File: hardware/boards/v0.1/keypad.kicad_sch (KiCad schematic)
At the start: 74 parts, among them SW1 TRIG1, SW10 TRIG10, SW11 TRIG11, SW12 TRIG12, SW13 TRIG13, SW14 TRIG14, SW15 TRIG15, SW16 TRIG16, SW17 MENU0, SW18 HELP, SW19 MENU1, SW2 TRIG2, SW20 MENU2, SW21 MENU3, SW3 TRIG3, SW4 TRIG4, SW5 TRIG5, SW6 TRIG6, SW7 TRIG7, SW8 TRIG8, SW9 TRIG9, U25 TCA8418RTWR

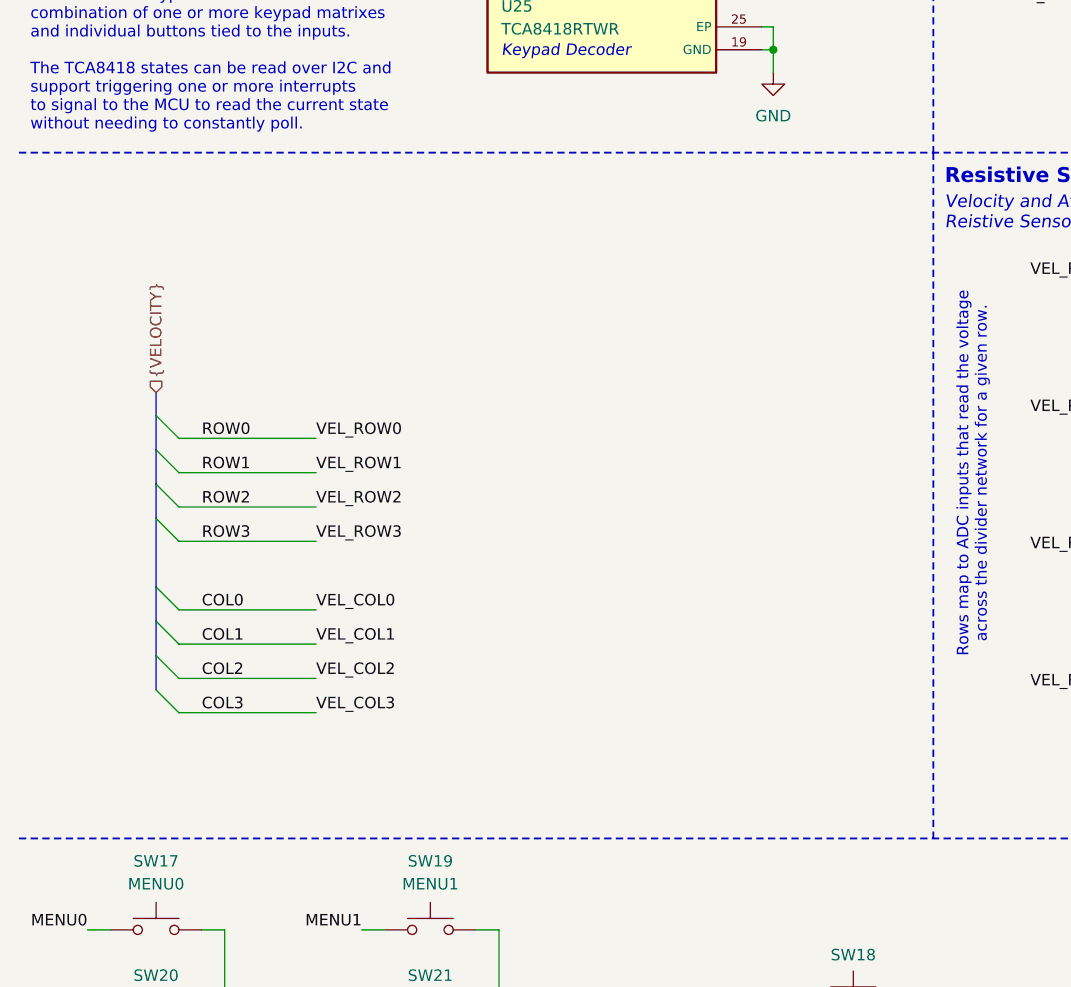
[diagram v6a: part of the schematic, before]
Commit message: feat: add IO expander for velocity pads
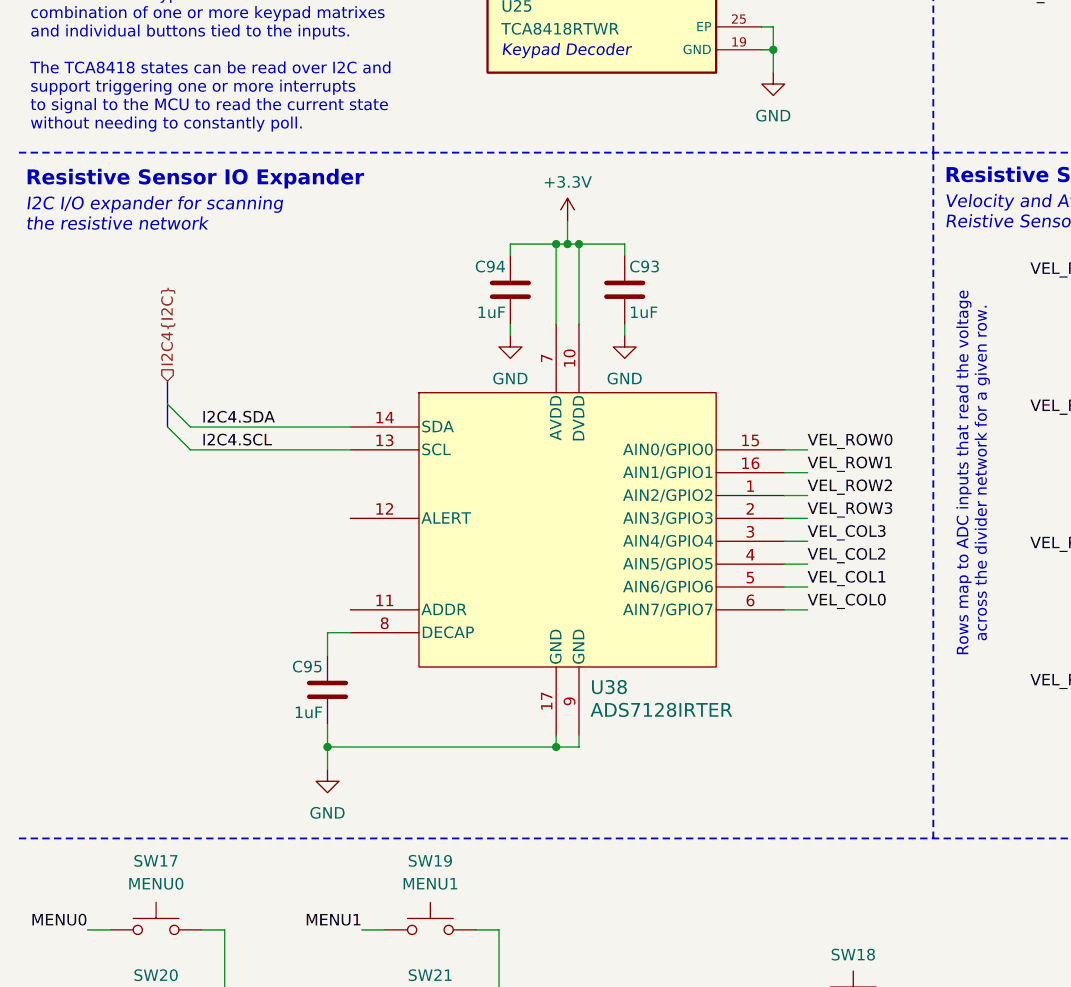
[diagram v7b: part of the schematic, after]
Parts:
- added C93, C94, C95: 1uF, Capacitor_SMD:C_0402_1005Metric, symbol Device:C
- added U38: ADS7128IRTER, pocket_synth:ADS7128IRTER, symbol pocket_synth:ADS7128IRTER
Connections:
- net +3.3V: now also C93.1, C94.1, U38.10 (DVDD), U38.7 (AVDD)
- net GND: now also C93.2, C94.2, C95.2, U38.17 (GND), U38.9 (GND)
- net I2C4.SCL: now also U38.13 (SCL)
- net I2C4.SDA: now also U38.14 (SDA)
- net COL0 renamed VEL_COL0
- net VEL_COL0: now also U38.6 (AIN7/GPIO7)
- net COL1 renamed VEL_COL1
- net VEL_COL1: now also U38.5 (AIN6/GPIO6)
- net COL2 renamed VEL_COL2
- net VEL_COL2: now also U38.4 (AIN5/GPIO5)
- net COL3 renamed VEL_COL3
- net VEL_COL3: now also U38.3 (AIN4/GPIO4)
- net ROW0 renamed VEL_ROW0
- net VEL_ROW0: now also U38.15 (AIN0/GPIO0)
- net ROW1 renamed VEL_ROW1
- net VEL_ROW1: now also U38.16 (AIN1/GPIO1)
- net ROW2 renamed VEL_ROW2
- net VEL_ROW2: now also U38.1 (AIN2/GPIO2)
- net ROW3 renamed VEL_ROW3
- net VEL_ROW3: now also U38.2 (AIN3/GPIO3)
- new net: C95.1, U38.8 (DECAP)
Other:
- note added: "I2C I/O expander for scanning the resistive network"
- note added: "Resistive Sensor IO Expander"

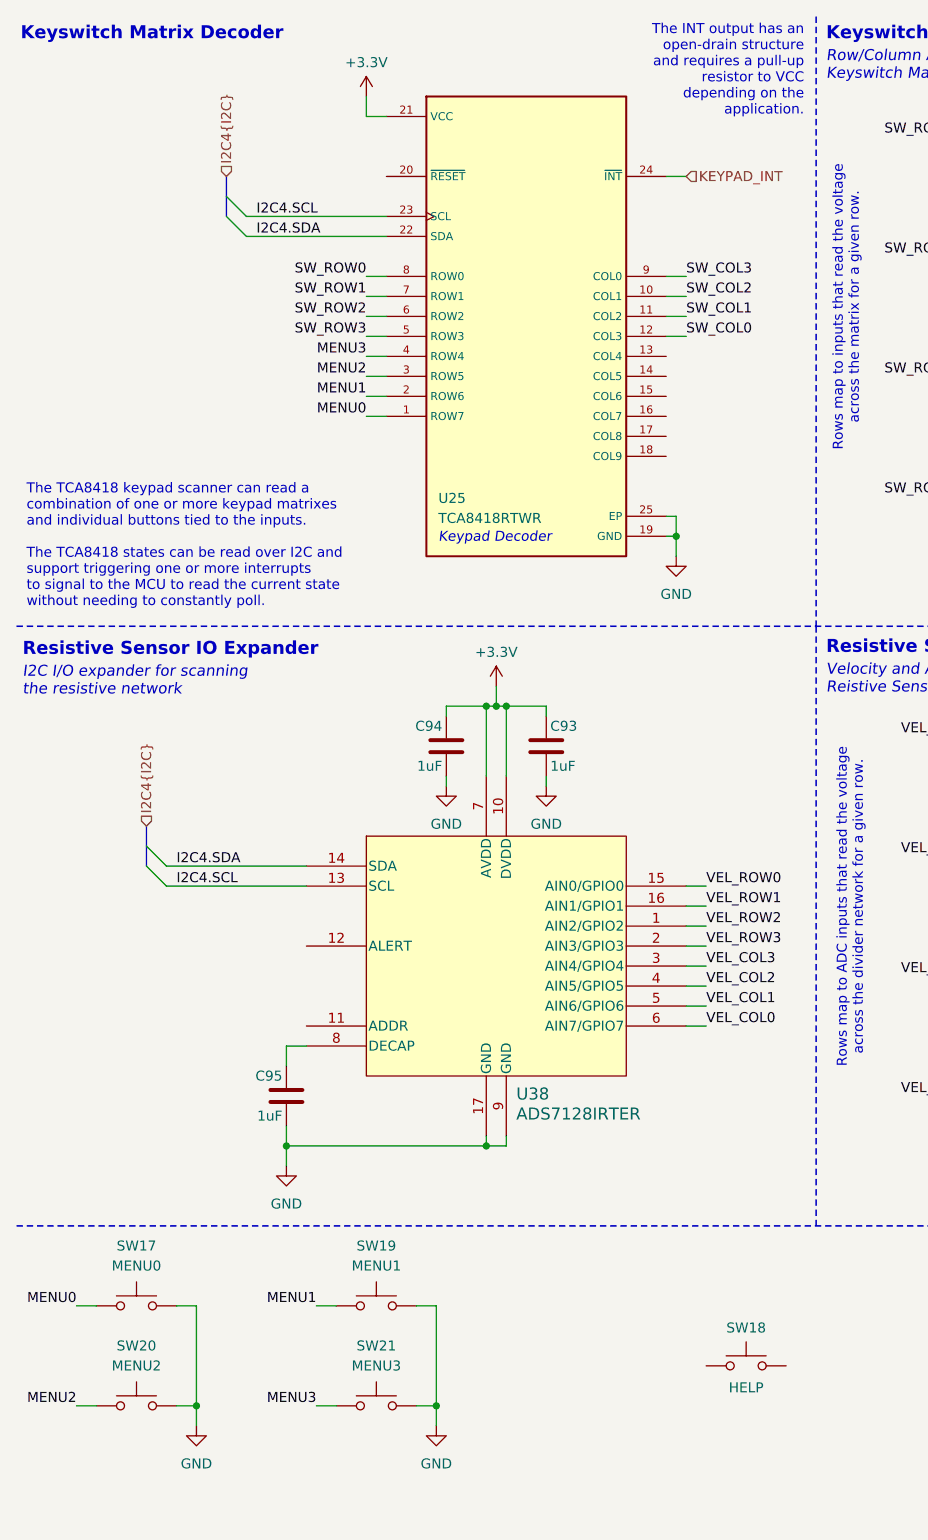
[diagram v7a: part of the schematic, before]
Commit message: feat: various ERC and DRC cleanup
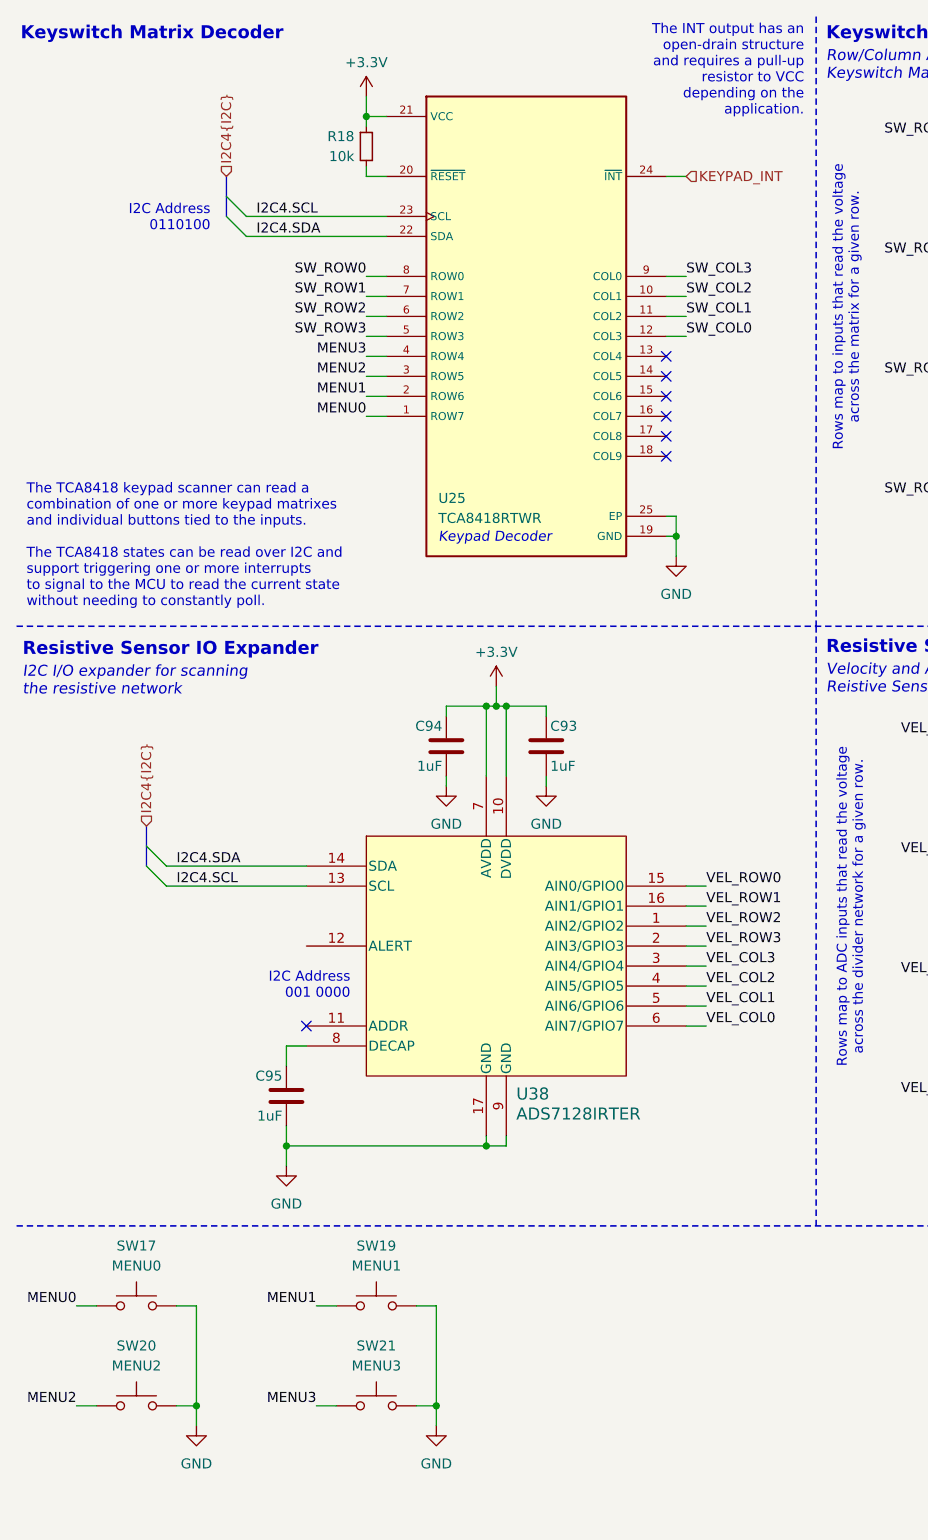
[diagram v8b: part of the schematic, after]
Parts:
- removed SW18: HELP, Button_Switch_SMD:SW_SPST_EVQQ2, symbol Switch:SW_Push
- added R18: 10k, Resistor_SMD:R_0402_1005Metric, symbol Device:R_Small
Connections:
- net +3.3V: now also R18.1
- net at U25.20 (~{RESET}): now also R18.2
- no-connect marks 0 -> 7
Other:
- note added: "I2C Address 001 0000"
- note added: "I2C Address 0110100"
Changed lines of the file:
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@@
 		)
 	)
+	(text "I2C Address\n001 0000"
+		(exclude_from_sim no)
+		(at 55.118 135.89 0)
+		(effects
+			(font
+				(size 1.27 1.27)
+				(color 132 132 132 1)
+			)
+			(justify right)
+		)
+	)
 	(text "Keyswitch Matrix Decoder"
 		(exclude_from_sim no)
@@
 		)
 	)
+	(text "I2C Address\n0110100"
+		(exclude_from_sim no)
+		(at 37.338 38.354 0)
+		(effects
+			(font
+				(size 1.27 1.27)
+				(color 132 132 132 1)
+			)
+			(justify right)
+		)
+	)
 	(text "TODO: add navigation stick?\nhttps://tech.alpsalpine.com/e/products/detail/RKJXT1F42001/#ancFig4"
 		(exclude_from_sim no)
@@
 	)
 	(junction
+		(at 57.15 25.4)
+		(diameter 0)
+		(color 0 0 0 0)
+	)
+	(junction
 		(at 135.89 43.18)
 		(diameter 0)
@@
 		(color 0 0 0 0)
 	)
+	(no_connect
+		(at 95.25 58.42)
+	)
+	(no_connect
+		(at 95.25 63.5)
+	)
+	(no_connect
+		(at 95.25 68.58)
+	)
+	(no_connect
+		(at 95.25 55.88)
+	)
+	(no_connect
+		(at 49.53 140.97)
+	)
+	(no_connect
+		(at 95.25 60.96)
+	)
+	(no_connect
+		(at 95.25 66.04)
+	)
 	(bus_entry
 		(at 41.91 38.1)
@@
 	(wire
 		(pts
+			(xy 57.15 25.4) (xy 57.15 26.67)
+		)
+		(stroke
+			(width 0)
+			(type default)
+		)
+	)
+	(wire
+		(pts
 			(xy 33.02 176.53) (xy 35.56 176.53)
 		)
@@
 	(wire
 		(pts
+			(xy 57.15 31.75) (xy 57.15 33.02)
+		)
+		(stroke
+			(width 0)
+			(type default)
+		)
+	)
+	(wire
+		(pts
 			(xy 195.58 127) (xy 196.85 127)
 		)
@@
 	(wire
 		(pts
+			(xy 57.15 33.02) (xy 59.69 33.02)
+		)
+		(stroke
+			(width 0)
+			(type default)
+		)
+	)
+	(wire
+		(pts
 			(xy 195.58 111.76) (xy 196.85 111.76)
 		)
@@
 	)
 	(symbol
-		(lib_id "Switch:SW_Push")
-		(at 105.41 184.15 0)
-		(unit 1)
-		(exclude_from_sim no)
-		(in_bom yes)
-		(on_board yes)
-		(dnp no)
-		(property "Reference" "SW18"
-			(at 105.41 179.324 0)
-			(effects
-				(font
-					(size 1.27 1.27)
-				)
-			)
-		)
-		(property "Value" "HELP"
-			(at 105.41 186.182 0)
-			(effects
-				(font
-					(size 1.27 1.27)
-				)
-				(justify top)
-			)
-		)
-		(property "Footprint" "Button_Switch_SMD:SW_SPST_EVQQ2"
-			(at 105.41 179.07 0)
-			(effects
-				(font
-					(size 1.27 1.27)
-				)
-				(hide yes)
-			)
-		)
-		(property "Datasheet" "~"
-			(at 105.41 179.07 0)
-			(effects
-				(font
-					(size 1.27 1.27)
-				)
-				(hide yes)
-			)
-		)
-		(property "Description" "Push button switch, generic, two pins"
-			(at 105.41 184.15 0)
-			(effects
-				(font
-					(size 1.27 1.27)
-				)
-				(hide yes)
-			)
-		)
-		(property "JLC" ""
-			(at 105.41 184.15 0)
-			(effects
-				(font
-					(size 1.27 1.27)
-				)
-			)
-		)
-		(property "Arrow Part Number" ""
-			(at 105.41 184.15 0)
-			(effects
-				(font
-					(size 1.27 1.27)
-				)
-			)
-		)
-		(property "Arrow Price/Stock" ""
-			(at 105.41 184.15 0)
-			(effects
-				(font
-					(size 1.27 1.27)
-				)
-			)
-		)
-		(property "MANUFACTURER" ""
-			(at 105.41 184.15 0)
-			(effects
-				(font
-					(size 1.27 1.27)
-				)
-			)
-		)
-		(property "MAXIMUM_PACKAGE_HEIGHT" ""
-			(at 105.41 184.15 0)
-			(effects
-				(font
-					(size 1.27 1.27)
-				)
-			)
-		)
-		(property "PARTREV" ""
-			(at 105.41 184.15 0)
-			(effects
-				(font
-					(size 1.27 1.27)
-				)
-			)
-		)
-		(property "STANDARD" ""
-			(at 105.41 184.15 0)
-			(effects
-				(font
-					(size 1.27 1.27)
-				)
-			)
-		)
-		(property "Connector" ""
-			(at 105.41 184.15 0)
-			(effects
-				(font
-					(size 1.27 1.27)
-				)
-			)
-		)
-		(pin "1"
-		)
-		(pin "2"
-		)
-		(instances
-			(project "pocket_synth"
-				(path "/485383b8-00f4-4405-b270-de249939cff4/7f1ac839-494f-4521-b63e-5606a3cb7bc9"
-					(reference "SW18")
-					(unit 1)
-				)
-			)
-		)
-	)
-	(symbol
 		(lib_id "Device:D")
 		(at 200.66 142.24 0)
@@
 					(unit 1)
 				)
+			)
+		)
+	)
+	(symbol
+		(lib_id "Device:R_Small")
+		(at 57.15 29.21 0)
+		(unit 1)
+		(exclude_from_sim no)
+		(in_bom yes)
+		(on_board yes)
+		(dnp no)
+		(property "Reference" "R18"
+			(at 55.626 27.94 0)
+			(effects
+				(font
+					(size 1.27 1.27)
+				)
+				(justify right)
+			)
+		)
+		(property "Value" "10k"
+			(at 55.626 30.48 0)
+			(effects
+				(font
+					(size 1.27 1.27)
+				)
+				(justify right)
+			)
+		)
+		(property "Footprint" "Resistor_SMD:R_0402_1005Metric"
+			(at 57.15 29.21 0)
+			(effects
+				(font
+					(size 1.27 1.27)
+				)
+				(hide yes)
+			)
+		)
+		(property "Datasheet" "~"
+			(at 57.15 29.21 0)
+			(effects
+				(font
+					(size 1.27 1.27)
+				)
+				(hide yes)
+			)
+		)
+		(property "Description" "Resistor, small symbol"
+			(at 57.15 29.21 0)
+			(effects
+				(font
+					(size 1.27 1.27)
+				)
+				(hide yes)
+			)
+		)
+		(pin "2"
+		)
+		(pin "1"
+		)
+		(instances
+			(project ""
+				(path "/485383b8-00f4-4405-b270-de249939cff4/7f1ac839-494f-4521-b63e-5606a3cb7bc9"
+					(reference "R18")
+					(unit 1)
+				)
